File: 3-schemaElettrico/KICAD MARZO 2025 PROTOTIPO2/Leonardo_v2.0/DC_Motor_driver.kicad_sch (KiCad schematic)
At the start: 0 parts

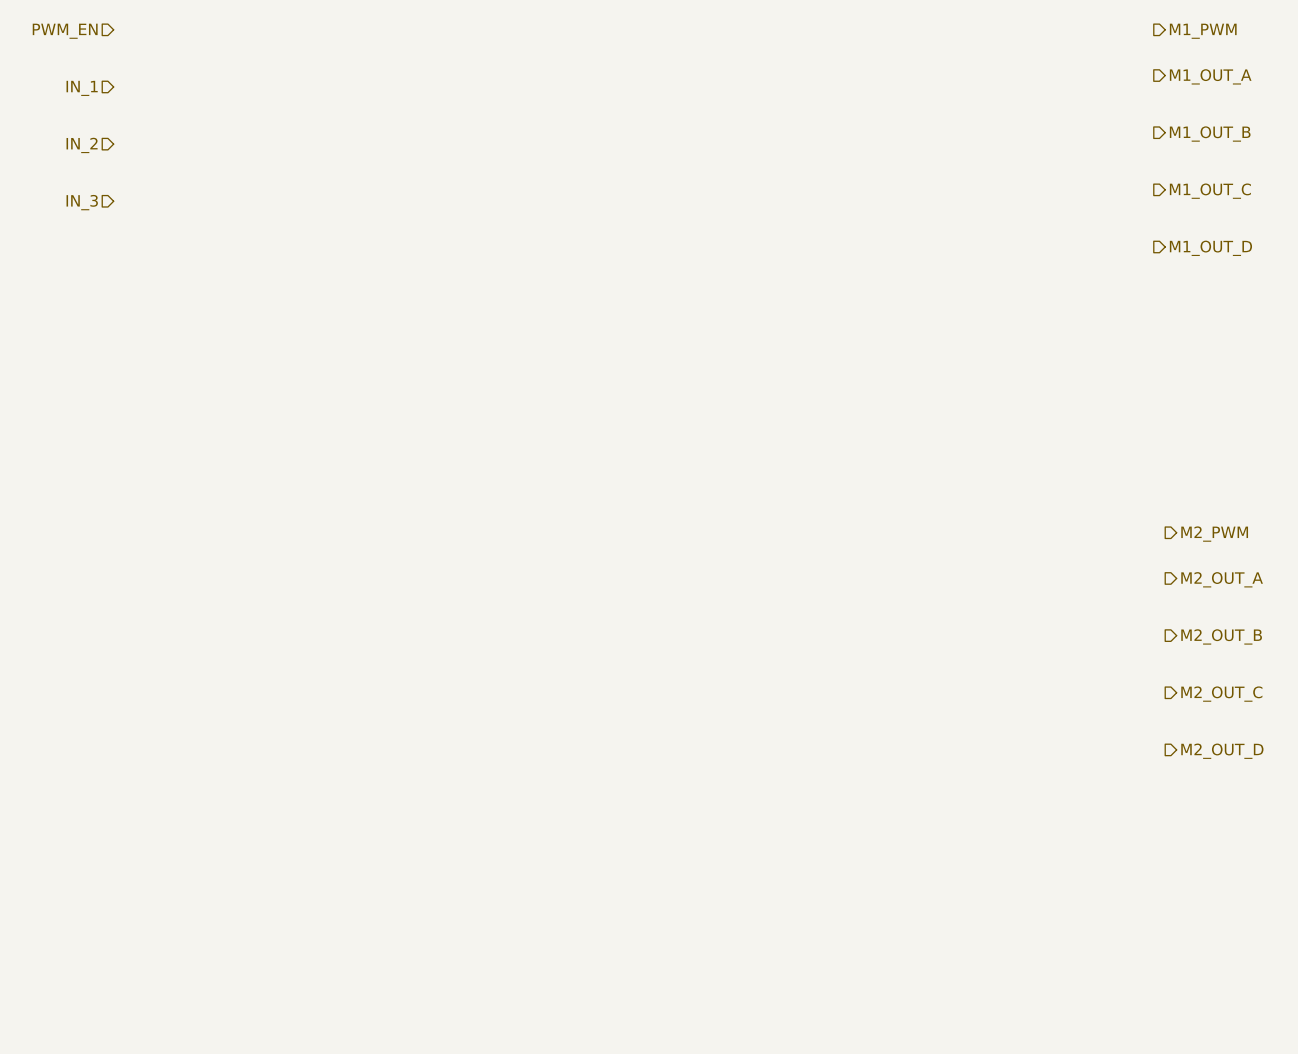
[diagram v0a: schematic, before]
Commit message: done 74hc238
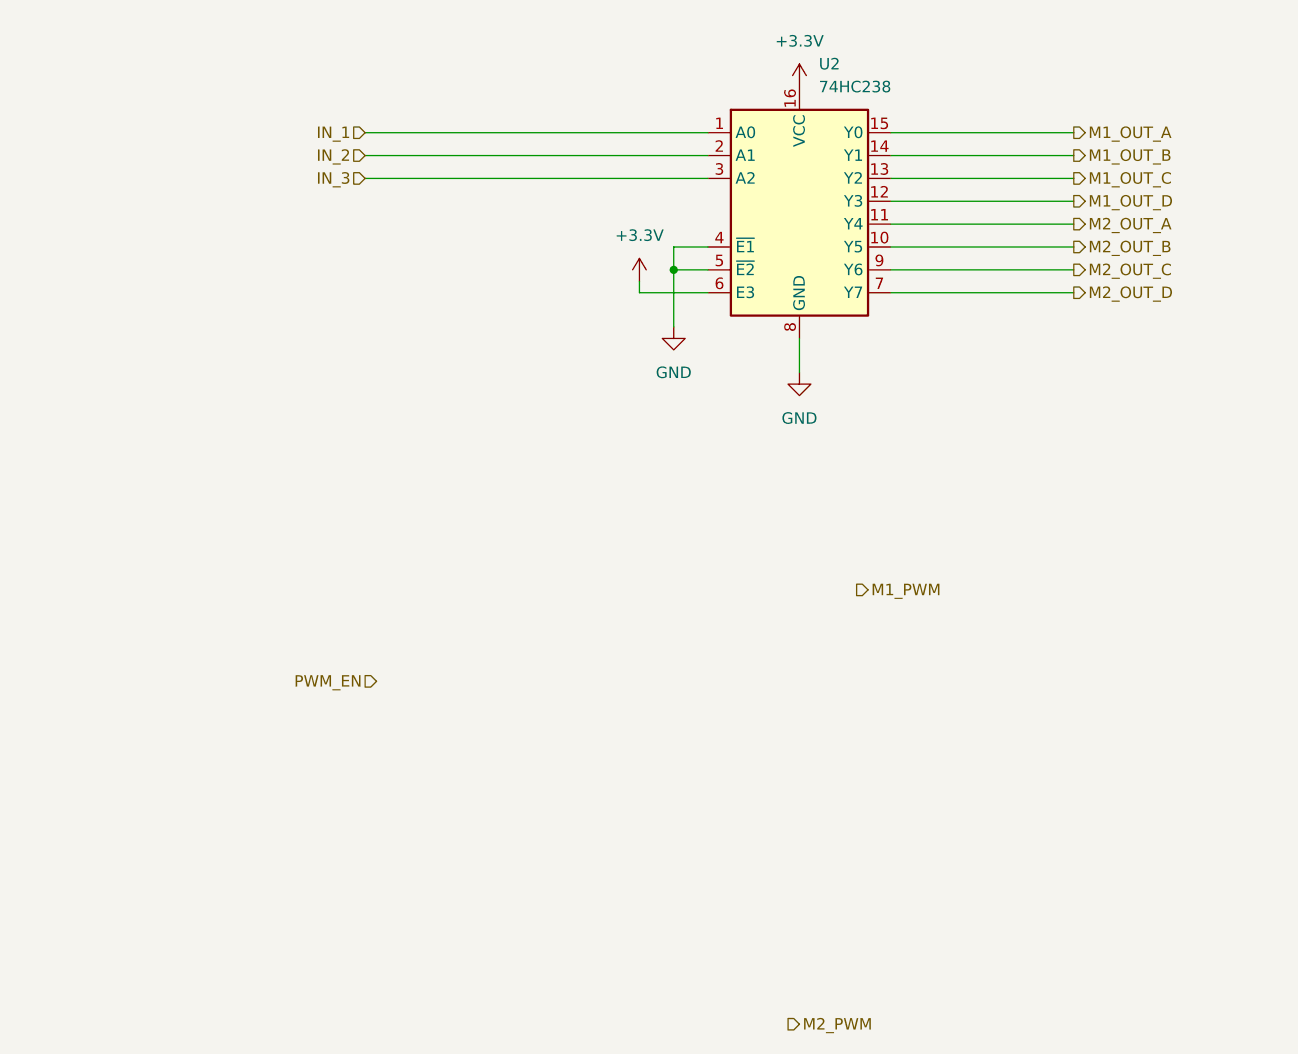
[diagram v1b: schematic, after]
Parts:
- added U2: 74HC238, symbol 74xx:74HC238
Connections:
- net IN_1: now also U2.1 (A0)
- net IN_2: now also U2.2 (A1)
- net IN_3: now also U2.3 (A2)
- net M1_OUT_A: now also U2.15 (Y0)
- net M1_OUT_B: now also U2.14 (Y1)
- net M1_OUT_C: now also U2.13 (Y2)
- net M1_OUT_D: now also U2.12 (Y3)
- net M2_OUT_A: now also U2.11 (Y4)
- net M2_OUT_B: now also U2.10 (Y5)
- net M2_OUT_C: now also U2.9 (Y6)
- net M2_OUT_D: now also U2.7 (Y7)
- new net +3.3V: U2.16 (VCC), U2.6 (E3)
- new net GND: U2.4 (~{E1}), U2.5 (~{E2}), U2.8 (GND)
